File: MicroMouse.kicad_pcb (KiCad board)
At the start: 2 copper layers, 100 x 80 mm, 78 parts, among them CN11 mouseBattery, Q1 IRLML6402, Q2 IRLML6344, SW1 SPST, SW2 SPST, SW3 SPST, U1 FULL_LED_A, U2 STM32F405RGTx, U3 TB6612, U4 CN_MOTOR, U5 CN_MOTOR, U6 MPU9250, U7 ZH

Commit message: 修正後
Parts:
- removed the REF** at (6.05, 0.13)
- removed the REF** at (6.05, 45.9)
- added REF**: motormount, myfootprint:motormount, F.Cu at (60.9, 12.0)
- added REF**: motormount, myfootprint:motormount, F.Cu at (60.9, 58.0)
- C1, C15, C16, C2, C4, C5: footprint myfootprint:GRM32EB31C476KE15 -> Resistors_SMD:R_1210_HandSoldering
- C10, C11, C13, C14, C9: footprint myfootprint:CL31A106KBHNNNE -> Resistors_SMD:R_0603_HandSoldering
- C17, C7, C8: footprint myfootprint:C1005X7R1H104K050BB -> Resistors_SMD:R_0603_HandSoldering
- D13, D5, D6, D7, D8: footprint myfootprint:OSTG1608C1A -> Resistors_SMD:R_0603_HandSoldering
- R1, R10, R11, R12, R13, R14, R15, R16, R17, R18, R19, R20, R21, R22, R23, R24, R25, R26, R27, R28, R29, R30, R31, R32, R6, R7, R8, R9: footprint Resistors_SMD:R_0402 -> Resistors_SMD:R_0603_HandSoldering
- moved R26 80.3 mm to (32.0, 55.0), turned to 180 degrees
- moved R27 77.5 mm to (32.0, 52.0), turned to 0 degrees
- moved R18 77.1 mm to (33.0, 60.0), turned to 270 degrees
- moved R19 76.2 mm to (30.0, 60.0), turned to 90 degrees
- moved C8 75.2 mm to (51.0, 32.0), turned to 180 degrees
- moved R21 73.8 mm to (24.5, 63.0), turned to 0 degrees
- moved R24 71.4 mm to (22.0, 41.0), turned to 180 degrees
- moved R23 68.8 mm to (26.0, 48.0), turned to 90 degrees
- moved R11 68.6 mm to (49.0, 55.0)
- moved R14 67.9 mm to (48.0, 69.0), turned to 0 degrees
- moved U1 67.6 mm to (46.0, 61.0)
- moved R10 67.1 mm to (46.0, 55.0)
- moved R28 66.9 mm to (94.0, 55.0), turned to 180 degrees
- moved SW2 66.6 mm to (48.0, 74.0), turned to 180 degrees
- moved R9 65.6 mm to (43.0, 55.0)
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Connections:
- C15 pad 2: Net-(C15-Pad2) -> GND
- C16 pad 2: Net-(C15-Pad2) -> GND
- C17 pad 2: Net-(C15-Pad2) -> GND
- REG2 pad 1: Net-(C15-Pad2) -> GND
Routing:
- net Net-(D10-Pad1): track 105.1 -> 22.4 mm, vias 9 -> 2
- net SPK: track 47.8 -> 99.0 mm, vias 2 -> 8
- net +5V: track 381.1 -> 342.1 mm, vias 48 -> 28
- net GND: track 502.1 -> 466.1 mm, vias 78 -> 42
- net USART1_RX: track 97.4 -> 65.1 mm, vias 8 -> 4
- net USART1_TX: track 95.8 -> 64.1 mm
- net Net-(D12-Pad2): track 51.3 -> 20.4 mm, vias 10 -> 0
- net Net-(D9-Pad2): track 77.9 -> 47.5 mm, vias 8 -> 4
- net SDA: track 50.8 -> 20.9 mm, vias 8 -> 2
- net Net-(U3-Pad5): track 71.7 -> 43.4 mm
- net LED_LF: track 41.6 -> 17.0 mm, vias 6 -> 2
- net M_STBY: track 54.9 -> 32.0 mm, vias 4 -> 2
- net M_IN2_R: track 55.0 -> 32.9 mm, vias 4 -> 6
- net LED_RF: track 57.6 -> 35.6 mm, vias 6 -> 4
- net Net-(D10-Pad2): track 47.3 -> 25.7 mm
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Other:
- rule via_min_size: 0.6 -> 0.4

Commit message: とりあえずコミット
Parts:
- removed R10, R9: 10, Resistors_SMD:R_0603_HandSoldering
- removed R11: 60.4, Resistors_SMD:R_0603_HandSoldering
- removed the REF** at (60.9, 12.0)
- removed the REF** at (60.9, 58.0)
- added C18: 0.1u, Resistors_SMD:R_0603_HandSoldering, F.Cu at (30.5, 26.7)
- added C19: 0.1u, Resistors_SMD:R_0603_HandSoldering, F.Cu at (44.5, 36.8)
- added C20: 0.1u, Resistors_SMD:R_0603_HandSoldering, F.Cu at (21.6, 35.6)
- added C21: 0.1u, Resistors_SMD:R_0603_HandSoldering, F.Cu at (31.8, 47.0)
- added D1: LED, Resistors_SMD:R_0603_HandSoldering, F.Cu at (2.54, 40.6)
- added D2: LED, Resistors_SMD:R_0603_HandSoldering, F.Cu at (10.2, 19.1)
- added R2: 280, Resistors_SMD:R_0603_HandSoldering, F.Cu at (-8.89, 34.3)
- added R3: 280, Resistors_SMD:R_0603_HandSoldering, F.Cu at (-2.54, 34.3)
- added REF**: motormount, myfootprint:motormount, F.Cu at (57.1, 12.7)
- added REF**: motormount, myfootprint:motormount, F.Cu at (54.6, 57.1)
- added U8: icm_right, Pin_Headers:Pin_Header_Straight_1x04, F.Cu at (52.1, 35.6)
- U1: value FULL_LED_A -> 3p; footprint myfootprint:OSTAMA5B31A -> Pin_Headers:Pin_Header_Straight_1x03
- U6: value MPU9250 -> 4p; footprint myfootprint:FH-1x5SG -> Pin_Headers:Pin_Header_Straight_1x04
- U7: value ZH -> icm_left; footprint myfootprint:B6B-ZR -> Pin_Headers:Pin_Header_Straight_1x04
- moved R20 58.2 mm to (52.1, -1.27)
- moved U5 57.1 mm to (90.2, 68.6), turned to 270 degrees
- moved U4 56.6 mm to (99.1, 11.4)
- moved U1 54.0 mm to (96.5, 41.9)
- moved R16 49.8 mm to (47.0, 1.27), turned to 0 degrees
- moved U7 48.0 mm to (52.1, 43.2)
- moved R17 45.2 mm to (39.4, -1.27)
- moved R14 43.4 mm to (83.8, 44.5)
- moved R6 41.4 mm to (-16.5, 39.4)
- moved SW2 41.4 mm to (83.8, 53.3)
- moved U6 40.3 mm to (96.5, 33.0), turned to 180 degrees
- moved C1 37.8 mm to (61.0, -2.54), turned to 0 degrees
- moved D7 36.4 mm to (20.3, 72.4), turned to 0 degrees
- moved R7 35.1 mm to (-10.2, 41.9)
- moved C2 34.5 mm to (64.8, 2.54), turned to 0 degrees
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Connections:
- C11 pad 1: +5V -> +3V3
- SP1 pad 2: +5V -> +3V3
- U1 pad 1: Net-(R9-Pad1) -> GND
- U1 pad 2: Net-(R10-Pad1) -> USART1_TX
- U1 pad 3: +3V3 -> USART1_RX
- U2 pad 2: Mode_LED_1 -> DBG_LED_4
- U2 pad 29: SCL -> SEN_RS
- U2 pad 3: Mode_LED_2 -> DBG_LED_5
- U2 pad 30: SDA -> SEN_RF
- U2 pad 33: Net-(U2-Pad33) -> CS
- U2 pad 4: Mode_LED_3 -> Net-(U2-Pad4)
- U2 pad 55: Net-(U2-Pad55) -> SCL
- U2 pad 56: SEN_RS -> SDO
- U2 pad 57: SEN_RF -> SDA
- U3 pad 20: +5V -> +3V3
- U6 pad 1: +3V3 -> GND
- U6 pad 2: +3V3 -> NRST
- U6 pad 3: SCL -> SWCLK
- U6 pad 4: SDA -> SWDIO
- U7 pad 1: GND -> +3V3
- U7 pad 2: NRST -> SCL
- U7 pad 3: SWCLK -> SDA
- U7 pad 4: SWDIO -> SDO
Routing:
- net GND: track 466.1 -> 0.00 mm, vias 42 -> 0
- net +5V: track 342.1 -> 0.00 mm, vias 28 -> 0
- net VCC: track 178.6 -> 0.00 mm, vias 10 -> 0
- net +3V3: track 173.9 -> 0.00 mm, vias 12 -> 0
- net NRST: track 102.9 -> 0.00 mm, vias 10 -> 0
- net SPK: track 99.0 -> 0.00 mm, vias 8 -> 0
- net SWCLK: track 91.1 -> 0.00 mm, vias 12 -> 0
- net SWDIO: track 70.0 -> 0.00 mm, vias 8 -> 0
- net L_ENC_B: track 66.6 -> 0.00 mm, vias 2 -> 0
- net R_ENC_A: track 65.2 -> 0.00 mm, vias 4 -> 0
- net USART1_RX: track 65.1 -> 0.00 mm, vias 4 -> 0
- net Net-(U3-Pad1): track 64.6 -> 0.00 mm, vias 8 -> 0
- net USART1_TX: track 64.1 -> 0.00 mm, vias 8 -> 0
- net L_ENC_A: track 63.7 -> 0.00 mm, vias 2 -> 0
- net R_ENC_B: track 62.4 -> 0.00 mm, vias 6 -> 0
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- removed copper zone on B.Cu, net GND
- removed copper zone on F.Cu, net GND

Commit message: GNDの配線だけした
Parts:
- removed the REF** at (57.1, 12.7)
- removed the REF** at (54.6, 57.1)
- removed U8: icm_right, Pin_Headers:Pin_Header_Straight_1x04
- added C22: 4.7u, Resistors_SMD:R_0603_HandSoldering, F.Cu at (29.0, 50.0)
- added REF**: motormount, myfootprint:motormount, F.Cu at (60.5, 12.0)
- added REF**: motormount, myfootprint:motormount, F.Cu at (60.5, 58.0)
- C12, C3, C6: footprint myfootprint:EEEHC1E470XP -> Capacitors_SMD:c_elec_6.3x7.7
- CN11: footprint myfootprint:DF3A-2P-2DSA -> RP_KiCAD_Connector:XA_2T
- OPAMP1, OPAMP2: footprint myfootprint:AD8532AR -> Housings_SOIC:SOIC-8_3.9x4.9mm_Pitch1.27mm
- Q1, Q2: footprint myfootprint:IRLML6402 -> myfootprint:SOT-23_Handsoldering
- REG1, REG2: footprint myfootprint:AZ1086 -> TO_SOT_Packages_SMD:SOT-223_reg
- SEN1, SEN2, SEN3, SEN4: footprint myfootprint:TSL262-R-LF-ND -> myfootprint:Socket_Strip_Straight_1x03
- U2: footprint myfootprint:STM32F405RGT6 -> myfootprint:LQFP-64_10x10mm_Pitch0.5mm
- U3: footprint myfootprint:TB6612FNG -> Housings_SSOP:SSOP-24_5.3x8.2mm_Pitch0.65mm
- U7: value icm_left -> ICM-20602; footprint Pin_Headers:Pin_Header_Straight_1x04 -> myfootprint:ICM-20602
- moved R6 53.4 mm to (25.4, 6.35)
- moved C5 50.9 mm to (43.0, 40.0)
- moved R8 44.2 mm to (24.1, 74.9), turned to 180 degrees
- moved C1 43.7 mm to (51.0, 40.0), turned to 180 degrees
- moved D13 41.8 mm to (61.0, 25.0), turned to 270 degrees
- moved R30 40.9 mm to (61.0, 30.0), turned to 90 degrees
- moved C4 36.8 mm to (43.0, 35.0)
- moved C2 35.3 mm to (51.0, 35.0), turned to 180 degrees
- moved R21 34.1 mm to (24.0, 53.0), turned to 90 degrees
- moved R18 31.6 mm to (22.0, 53.0), turned to 270 degrees
- moved R20 31.5 mm to (24.0, 13.0), turned to 90 degrees
- moved R16 27.6 mm to (22.0, 13.0), turned to 270 degrees
- moved R7 26.9 mm to (8.89, 61.0), turned to 180 degrees
- moved C15 25.8 mm to (51.0, 45.0), turned to 180 degrees
- moved C12 22.1 mm to (85.0, 6.00), turned to 270 degrees
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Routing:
- net GND: track 0.00 -> 462.0 mm, vias 0 -> 2

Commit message: 向き調整
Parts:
- moved C12 21.6 mm to (90.0, 27.0)
- moved C13 12.7 mm to (90.0, 34.0), turned to 270 degrees
- moved C14 8.49 mm to (87.0, 34.0), turned to 270 degrees
- moved R6 3.30 mm to (28.4, 5.08)
- moved D5 2.96 mm to (33.0, 5.33), turned to 180 degrees
- moved C11 1.00 mm to (81.0, 30.0), turned to 0 degrees
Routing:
- net +3V3: track 0.00 -> 116.4 mm, vias 0 -> 6
- net +5V: track 0.00 -> 106.8 mm, vias 0 -> 6
- net GND: track 462.0 -> 368.8 mm
- net VCC: track 0.00 -> 75.9 mm, vias 0 -> 4
- net Net-(CN11-Pad1): track 0.00 -> 10.5 mm, vias 0 -> 2

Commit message: 昔の確認
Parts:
- removed C20, C21: 0.1u, Resistors_SMD:R_0603_HandSoldering
- removed C22: 4.7u, Resistors_SMD:R_0603_HandSoldering
- removed CN11: mouseBattery, RP_KiCAD_Connector:XA_2T
- removed D12: LED_LF, LEDs:LED-5MM
- removed D13: LED, Resistors_SMD:R_0603_HandSoldering
- removed R28, R31, R32: 10k, Resistors_SMD:R_0603_HandSoldering
- removed R29: 10, Resistors_SMD:R_0603_HandSoldering
- removed R30: 280, Resistors_SMD:R_0603_HandSoldering
- added CN1: mouseBattery, RP_KiCAD_Connector:XA_2T, F.Cu at (56.0, 17.0)
- added D3: LED, Resistors_SMD:R_0603_HandSoldering, F.Cu at (59.9, 86.4)
- added D4: LED, Resistors_SMD:R_0603_HandSoldering, F.Cu at (60.5, 94.0)
- added R10: 10k, Resistors_SMD:R_0603_HandSoldering, F.Cu at (37.6, 48.8)
- added R11: 2.7k, Resistors_SMD:R_0603_HandSoldering, F.Cu at (40.1, 45.2)
- added R4: 280, Resistors_SMD:R_0603_HandSoldering, F.Cu at (53.8, 97.5)
- added R5: 280, Resistors_SMD:R_0603_HandSoldering, F.Cu at (29.5, 88.9)
- added R9: 10k, Resistors_SMD:R_0603_HandSoldering, F.Cu at (85.0, 49.0)
- C1, C15, C2: value 47u -> 10u; footprint Resistors_SMD:R_1210_HandSoldering -> Resistors_SMD:R_0603_HandSoldering
- C10: value 10u -> 4.7u
- C11: value 10u -> 2.2u
- C12: value 47u -> 2.2u; footprint Capacitors_SMD:c_elec_6.3x7.7 -> Resistors_SMD:R_0603_HandSoldering
- C16: footprint Resistors_SMD:R_1210_HandSoldering -> Capacitors_SMD:c_elec_6.3x7.7
- C17, C18, C19: value 0.1u -> 10u
- C3: value 47u -> 22u; footprint Capacitors_SMD:c_elec_6.3x7.7 -> Resistors_SMD:R_0603_HandSoldering
- C4: value 47u -> 22u; footprint Resistors_SMD:R_1210_HandSoldering -> Resistors_SMD:R_0603_HandSoldering
- C5: value 47u -> 0.1u; footprint Resistors_SMD:R_1210_HandSoldering -> Resistors_SMD:R_0603_HandSoldering
- C6: value 47u -> 0.1u; footprint Capacitors_SMD:c_elec_6.3x7.7 -> Resistors_SMD:R_0603_HandSoldering
- C7, C8: value 2.2u -> 0.1u
- C9: value 10u -> 0.1u
- D10: value LED_LS -> LED_RF
- D11: value LED_RF -> LED_LF
- D8: value LED -> LED_RS; footprint Resistors_SMD:R_0603_HandSoldering -> LEDs:LED-5MM
- D9: value LED_RS -> LED_LS
- R12: value 620 -> 5.76k
- R13: value 10k -> 2.7k
- R14: value 10k -> 5.76k
- R16, R18, R24: value 5.76k -> 10
- R17, R19: value 2.7k -> 10
- R20, R22: value 10 -> 5.76k
- R21, R23: value 10 -> 2.7k
- R25, R27: value 2.7k -> 10k
- R26: value 5.76k -> 10k
- R8: value 280 -> 620
- U1: value 3p -> STM32F405RGTx; footprint Pin_Headers:Pin_Header_Straight_1x03 -> myfootprint:LQFP-64_10x10mm_Pitch0.5mm
- U2: value STM32F405RGTx -> TB6612; footprint myfootprint:LQFP-64_10x10mm_Pitch0.5mm -> Housings_SSOP:SSOP-24_5.3x8.2mm_Pitch0.65mm
- U3: value TB6612 -> CN_MOTOR; footprint Housings_SSOP:SSOP-24_5.3x8.2mm_Pitch0.65mm -> myfootprint:BH-10SG
- U5: value CN_MOTOR -> 3p; footprint myfootprint:BH-10SG -> Pin_Headers:Pin_Header_Straight_1x03
- U6: value 4p -> ICM-20602; footprint Pin_Headers:Pin_Header_Straight_1x04 -> myfootprint:ICM-20602
- U7: value ICM-20602 -> 4p; footprint myfootprint:ICM-20602 -> Pin_Headers:Pin_Header_Straight_1x04
- moved R25 74.7 mm to (88.0, 62.0), turned to 0 degrees
- moved R24 70.5 mm to (88.0, 59.0), turned to 0 degrees
- moved D9 70.0 mm to (40.0, 76.0)
- moved U1 69.0 mm to (28.0, 40.0), turned to 45 degrees
- moved C13 65.4 mm to (33.0, 66.0)
- moved U4 58.1 mm to (95.0, 69.0)
- moved R26 57.1 mm to (85.0, 55.0), turned to 180 degrees
- moved U2 57.0 mm to (80.0, 40.0), turned to 180 degrees
- moved C12 56.6 mm to (33.5, 31.0), turned to 0 degrees
- moved C14 55.3 mm to (33.0, 22.0)
- moved D10 54.9 mm to (12.0, 28.0), turned to 45 degrees
- moved R14 48.5 mm to (33.0, 56.0), turned to 270 degrees
- moved C18 44.2 mm to (71.0, 33.0), turned to 90 degrees
- moved C11 44.2 mm to (37.1, 34.5)
- moved R22 42.0 mm to (24.0, 69.0), turned to 90 degrees
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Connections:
- C10 pad 1: +5V -> +3V3
- C11 pad 1: +3V3 -> GND
- C11 pad 2: GND -> Net-(C11-Pad2)
- C12 pad 1: VCC -> GND
- C12 pad 2: GND -> Net-(C12-Pad2)
- C13 pad 1: VCC -> +5V
- C14 pad 1: VCC -> +5V
- C15 pad 1: VCC -> +3V3
- C16 pad 1: +3V3 -> VCC
- C17 pad 1: +3V3 -> VCC
- C18 pad 1: +3V3 -> VCC
- C3 pad 1: VCC -> +5V
- C4 pad 1: +5V -> +3V3
- C5 pad 1: +5V -> +3V3
- C6 pad 1: +5V -> +3V3
- C7 pad 1: GND -> +3V3
- C7 pad 2: Net-(C7-Pad2) -> GND
- C8 pad 1: GND -> +3V3
- C8 pad 2: Net-(C8-Pad2) -> GND
- C9 pad 1: +5V -> +3V3
- D1 pad 1: DBG_LED_4 -> DBG_LED_1
- D2 pad 1: DBG_LED_5 -> DBG_LED_2
- D5 pad 1: DBG_LED_1 -> DBG_LED_5
- D6 pad 1: DBG_LED_2 -> GND
- D7 pad 1: DBG_LED_3 -> GND
- D8 pad 1: GND -> Net-(D8-Pad1)
- OPAMP1 pad 1: Net-(D9-Pad2) -> Net-(D8-Pad2)
- OPAMP1 pad 2: Net-(D9-Pad1) -> Net-(D8-Pad1)
- OPAMP1 pad 6: Net-(D11-Pad1) -> Net-(D10-Pad1)
- OPAMP1 pad 7: Net-(D11-Pad2) -> Net-(D10-Pad2)
- OPAMP2 pad 1: Net-(D10-Pad2) -> Net-(D9-Pad2)
- OPAMP2 pad 2: Net-(D10-Pad1) -> Net-(D9-Pad1)
- OPAMP2 pad 6: Net-(D12-Pad1) -> Net-(D11-Pad1)
- OPAMP2 pad 7: Net-(D12-Pad2) -> Net-(D11-Pad2)
- R12 pad 1: +5V -> LED_RS
- R12 pad 2: Net-(D8-Pad2) -> Net-(OPAMP1-Pad3)
- R13 pad 1: SEN_BAT -> Net-(OPAMP1-Pad3)
- R13 pad 2: VCC -> GND
- R14 pad 1: Mode_SW -> LED_LS
- R14 pad 2: +3V3 -> Net-(OPAMP2-Pad3)
- R15 pad 1: GND -> Net-(OPAMP2-Pad3)
- R15 pad 2: SEN_BAT -> GND
- R16 pad 1: LED_RS -> Net-(D8-Pad1)
- R16 pad 2: Net-(OPAMP1-Pad3) -> GND
- R17 pad 1: Net-(OPAMP1-Pad3) -> Net-(D9-Pad1)
- R18 pad 1: LED_LS -> Net-(D10-Pad1)
- R18 pad 2: Net-(OPAMP2-Pad3) -> GND
- R19 pad 1: Net-(OPAMP2-Pad3) -> Net-(D11-Pad1)
- R20 pad 1: Net-(D9-Pad1) -> LED_RF
- R20 pad 2: GND -> Net-(OPAMP1-Pad5)
- R21 pad 1: Net-(D10-Pad1) -> Net-(OPAMP1-Pad5)
- R22 pad 1: Net-(D11-Pad1) -> LED_LF
- R22 pad 2: GND -> Net-(OPAMP2-Pad5)
- R23 pad 1: Net-(D12-Pad1) -> Net-(OPAMP2-Pad5)
- R24 pad 1: LED_RF -> SPK
- R24 pad 2: Net-(OPAMP1-Pad5) -> Net-(Q2-Pad1)
- R25 pad 1: Net-(OPAMP1-Pad5) -> GND
- R25 pad 2: GND -> Net-(Q2-Pad1)
- R26 pad 1: LED_LF -> NRST
- R26 pad 2: Net-(OPAMP2-Pad5) -> +3V3
- R27 pad 1: Net-(OPAMP2-Pad5) -> BOOT0
- R8 pad 1: +3V3 -> +5V
- U1 pad 1: GND -> +3V3
- U1 pad 2: USART1_TX -> DBG_LED_4
- U1 pad 3: USART1_RX -> DBG_LED_5
- U2 pad 1: +3V3 -> Net-(U2-Pad1)
- U2 pad 10: LED_LF -> GND
- U2 pad 11: LED_LS -> Net-(U2-Pad11)
- U2 pad 12: GND -> Net-(U2-Pad11)
- U2 pad 13: +3V3 -> VCC
- U2 pad 14: Net-(U2-Pad14) -> VCC
- U2 pad 15: Net-(U2-Pad15) -> M_PWM_R
- U2 pad 16: M_PWM_R -> M_IN2_R
- U2 pad 17: M_PWM_L -> M_IN1_R
- U2 pad 19: +3V3 -> M_STBY
- U2 pad 2: DBG_LED_4 -> Net-(U2-Pad1)
- U2 pad 20: SEN_BAT -> +3V3
- U2 pad 21: SPK -> M_IN1_L
- U2 pad 22: R_ENC_A -> M_IN2_L
- U2 pad 23: R_ENC_B -> M_PWM_L
- U2 pad 24: M_IN1_R -> VCC
- U2 pad 3: DBG_LED_5 -> GND
- U2 pad 4: Net-(U2-Pad4) -> GND
- U2 pad 6: Net-(U2-Pad6) -> Net-(U2-Pad5)
- U2 pad 7: NRST -> Net-(U2-Pad7)
- U2 pad 8: LED_RS -> Net-(U2-Pad7)
- U2 pad 9: LED_RF -> GND
- U3 pad 1: Net-(U3-Pad1) -> Net-(U2-Pad11)
- U3 pad 10: GND -> Net-(U3-Pad10)
- U3 pad 2: Net-(U3-Pad1) -> +5V
- U3 pad 4: GND -> Net-(U2-Pad7)
- U3 pad 6: Net-(U3-Pad5) -> R_ENC_A
- U3 pad 8: Net-(U3-Pad7) -> R_ENC_B
- U3 pad 9: GND -> Net-(U3-Pad9)
- U4 pad 1: Net-(U3-Pad11) -> Net-(U2-Pad5)
- U4 pad 4: Net-(U3-Pad7) -> Net-(U2-Pad1)
- U4 pad 6: R_ENC_A -> L_ENC_A
- U4 pad 8: R_ENC_B -> L_ENC_B
- U5 pad 1: Net-(U3-Pad5) -> GND
- U5 pad 2: +5V -> USART1_TX
- U5 pad 3: GND -> USART1_RX
- U6 pad 1: GND -> +3V3
- U6 pad 2: NRST -> SCL
- U6 pad 3: SWCLK -> SDA
- U6 pad 4: SWDIO -> SDO
- U7 pad 1: +3V3 -> GND
- U7 pad 2: SCL -> NRST
- U7 pad 3: SDA -> SWCLK
- U7 pad 4: SDO -> SWDIO
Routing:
- net GND: track 368.8 -> 280.7 mm, vias 2 -> 0
- net +3V3: track 116.4 -> 62.8 mm, vias 6 -> 2
- net VCC: track 75.9 -> 31.4 mm, vias 4 -> 2
- net Net-(D9-Pad1): track 0.00 -> 28.6 mm, vias 0 -> 4
- net Net-(D11-Pad2): track 0.00 -> 27.4 mm, vias 0 -> 2
- net Net-(D11-Pad1): track 0.00 -> 26.3 mm, vias 0 -> 2
- net +5V: track 106.8 -> 130.7 mm, vias 6 -> 1
- net Net-(D9-Pad2): track 0.00 -> 21.4 mm, vias 0 -> 2
- net Net-(D10-Pad1): track 0.00 -> 21.2 mm, vias 0 -> 2
- net Net-(D8-Pad1): track 0.00 -> 19.4 mm
- net Net-(D10-Pad2): track 0.00 -> 17.7 mm, vias 0 -> 2
- net Net-(D8-Pad2): track 0.00 -> 15.5 mm
- net Net-(OPAMP1-Pad3): track 0.00 -> 10.2 mm, vias 0 -> 2
- net Net-(Q1-Pad1): track 0.00 -> 9.76 mm
- net Net-(OPAMP2-Pad3): track 0.00 -> 9.02 mm
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
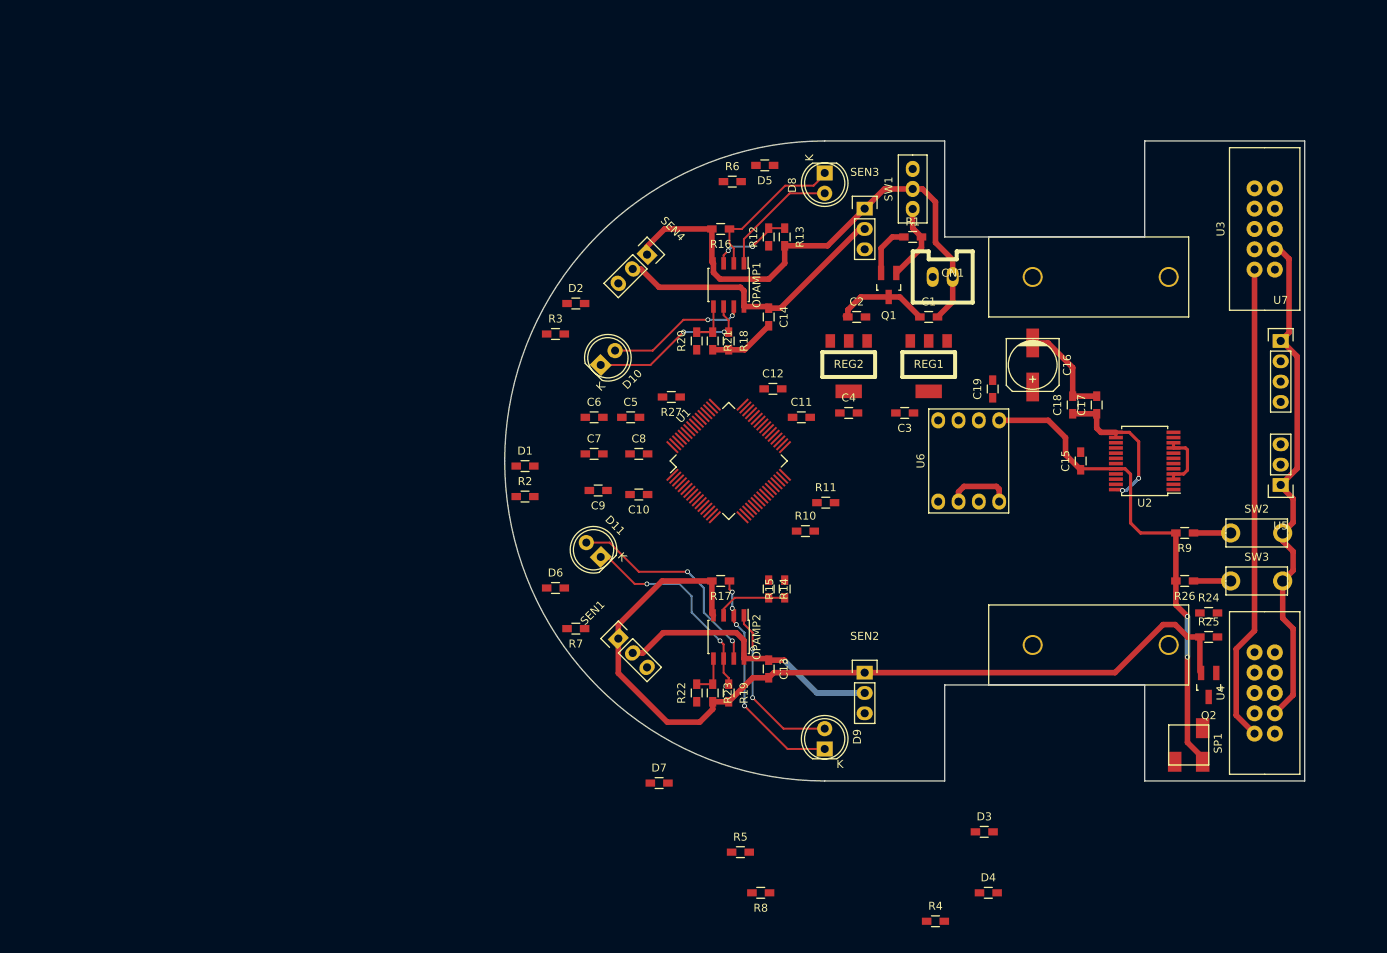
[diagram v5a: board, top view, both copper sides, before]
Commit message: ピン変えました
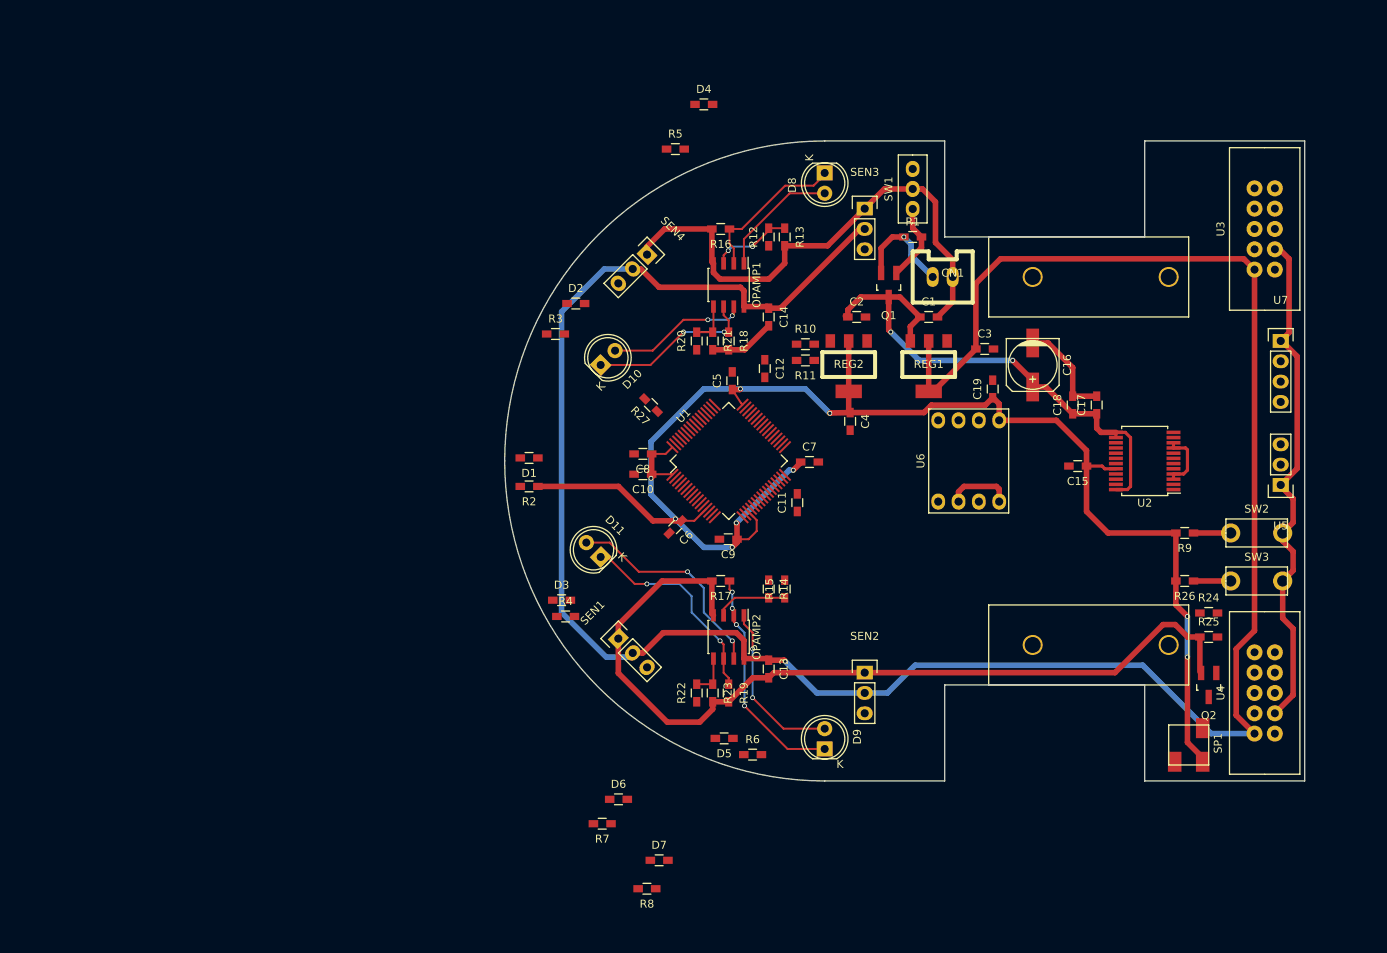
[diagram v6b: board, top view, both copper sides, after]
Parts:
- moved D4 104.8 mm to (24.9, -4.57)
- moved R5 88.3 mm to (21.3, 1.02)
- moved D5 71.8 mm to (27.4, 74.7)
- moved R6 71.7 mm to (31.0, 76.7)
- moved D3 60.2 mm to (7.11, 57.4)
- moved R4 59.9 mm to (7.62, 59.4)
- moved D6 27.6 mm to (14.2, 82.3)
- moved C7 26.9 mm to (38.1, 40.1)
- moved R7 24.6 mm to (12.2, 85.3)
- moved R10 23.4 mm to (37.6, 25.4)
- moved R11 18.0 mm to (37.6, 27.4), turned to 180 degrees
- moved C9 17.4 mm to (27.9, 49.8)
- moved C6 17.1 mm to (21.3, 48.3), turned to 225 degrees
- moved R8 14.2 mm to (17.8, 93.5)
- moved C5 13.5 mm to (28.4, 30.0), turned to 90 degrees
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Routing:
- net +5V: track 130.7 -> 303.8 mm
- net +3V3: track 62.8 -> 202.2 mm, vias 2 -> 9
- net VCC: track 31.4 -> 66.3 mm
- net Net-(CN1-Pad1): track 6.53 -> 13.0 mm, vias 0 -> 1
